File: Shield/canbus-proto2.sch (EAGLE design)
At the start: 81 parts, among them J1 Digital_0_7, J2 Analog, J3 Digital_8_13, J4 Analog, J5 Digital_14_21

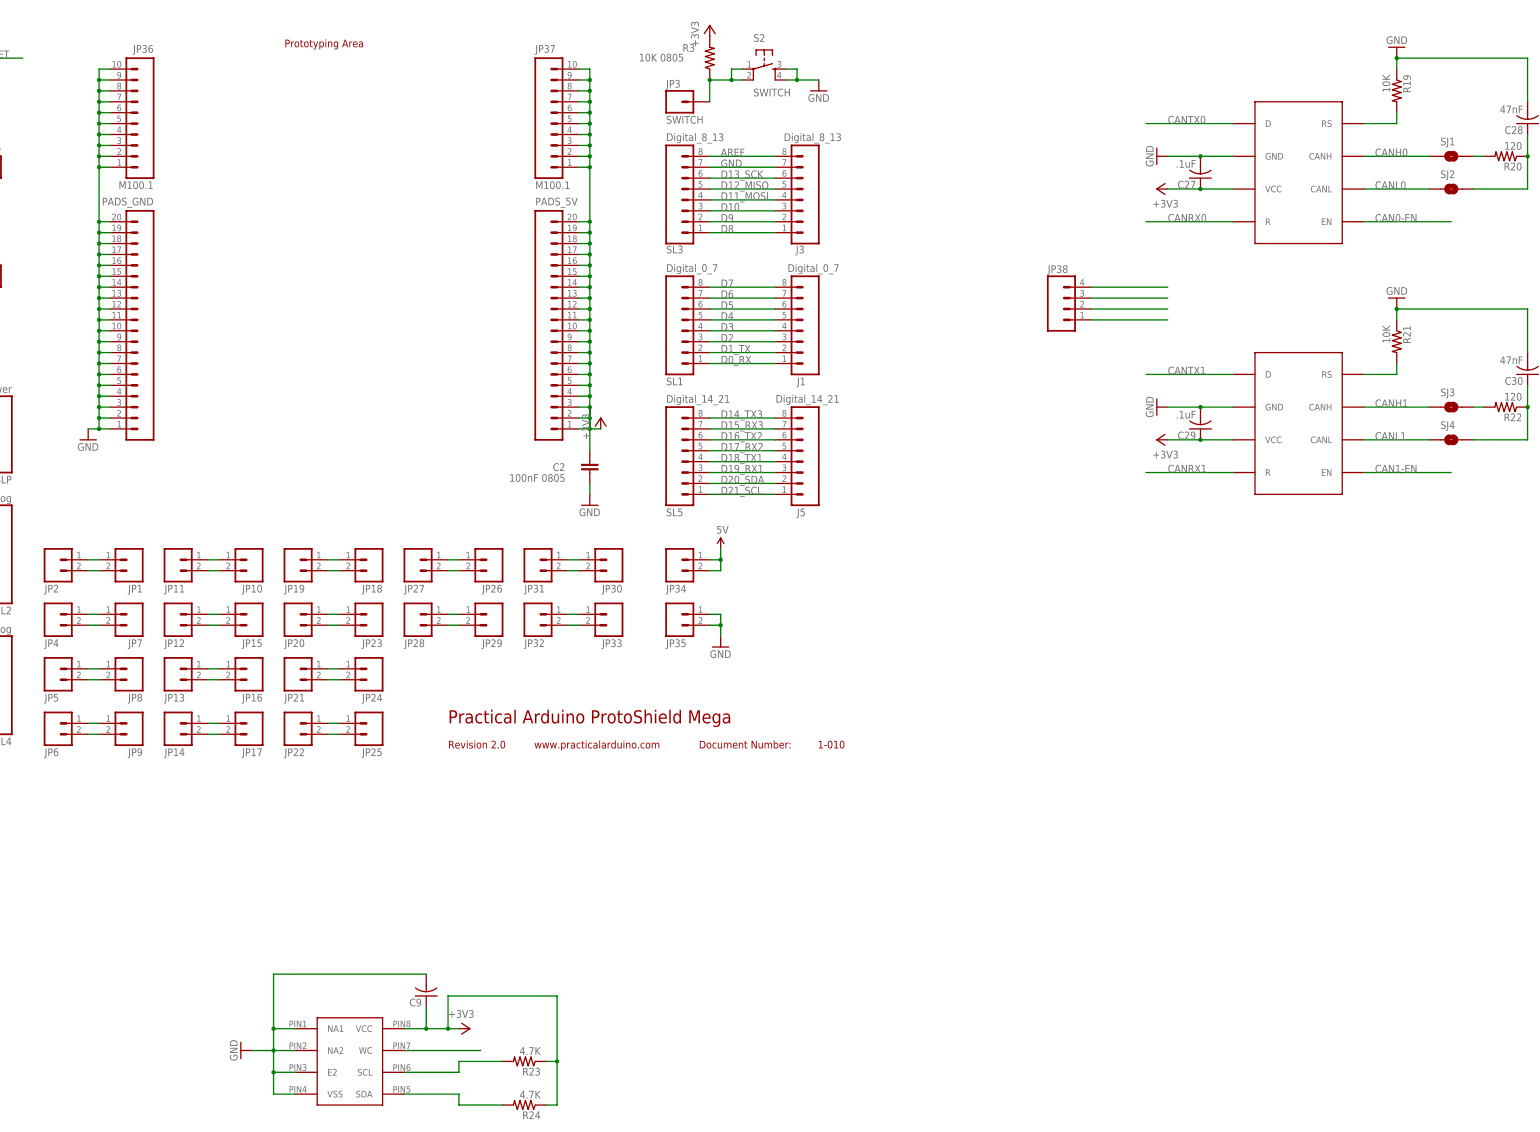
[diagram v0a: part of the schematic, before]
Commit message: Updated board design for canbus shield. There are now RJ45 ports for canbus outputs and a little SMD proto space.
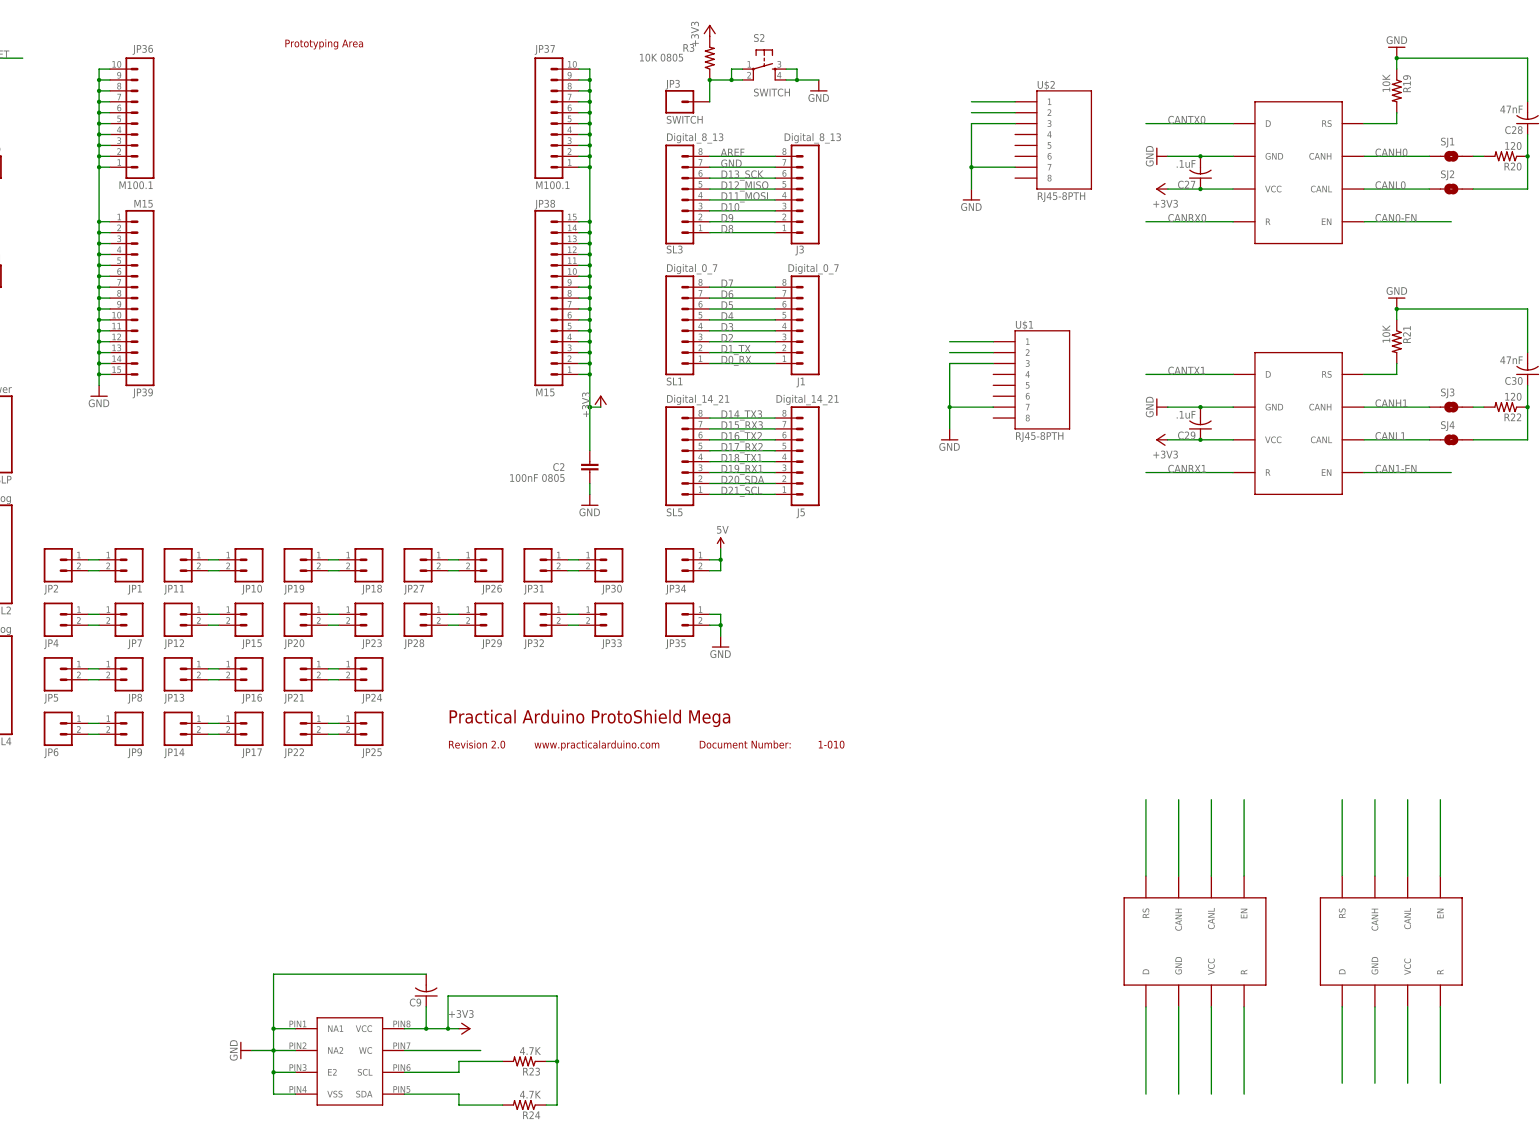
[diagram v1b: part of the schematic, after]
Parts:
- removed PADS_5V, PADS_GND: M20, SparkFun:M20
- added JP39: M15, SparkFun-Connectors:M15
- added U$1, U$2: RJ45-8PTH, SparkFun-Connectors:RJ45-8PTH
- added U$3, U$4: SN65HVD234, ck_custom:SN65HVD234
- JP38: value (none) -> M15; device SparkFun-Connectors:M04PTH -> SparkFun-Connectors:M15
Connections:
- new net B1: U$3.RS
- new net B10: U$4.CANH
- new net B11: U$4.CANL
- new net B12: U$4.EN
- new net B13: U$4.R
- new net B14: U$4.VCC
- new net B15: U$4.GND
- new net B16: U$4.D
- new net B2: U$3.CANH
- new net B3: U$3.CANL
- new net B4: U$3.EN
- new net B5: U$3.D
- new net B6: U$3.GND
- new net B7: U$3.VCC
- new net B8: U$3.R
- new net B9: U$4.RS
- net +3V3: now also JP38.1, JP38.10, JP38.11, JP38.12, JP38.13, JP38.14, JP38.15, JP38.2, JP38.3, JP38.4, JP38.5, JP38.6, JP38.7, JP38.8, JP38.9; no longer PADS_5V.1, PADS_5V.10, PADS_5V.11, PADS_5V.12, PADS_5V.13, PADS_5V.14, PADS_5V.15, PADS_5V.16, PADS_5V.17, PADS_5V.18, PADS_5V.19, PADS_5V.2, PADS_5V.20, PADS_5V.3, PADS_5V.4, PADS_5V.5, PADS_5V.6, PADS_5V.7, PADS_5V.8, PADS_5V.9
- net CANH0: now also U$2.1; no longer JP38.2
- net CANH1: now also U$1.1; no longer JP38.4
- net CANL0: now also U$2.2; no longer JP38.1
- net CANL1: now also U$1.2; no longer JP38.3
- net GND: now also JP39.1, JP39.10, JP39.11, JP39.12, JP39.13, JP39.14, JP39.15, JP39.2, JP39.3, JP39.4, JP39.5, JP39.6, JP39.7, JP39.8, JP39.9, U$1.3, U$1.7, U$2.3, U$2.7; no longer PADS_GND.1, PADS_GND.10, PADS_GND.11, PADS_GND.12, PADS_GND.13, PADS_GND.14, PADS_GND.15, PADS_GND.16, PADS_GND.17, PADS_GND.18, PADS_GND.19, PADS_GND.2, PADS_GND.20, PADS_GND.3, PADS_GND.4, PADS_GND.5, PADS_GND.6, PADS_GND.7, PADS_GND.8, PADS_GND.9

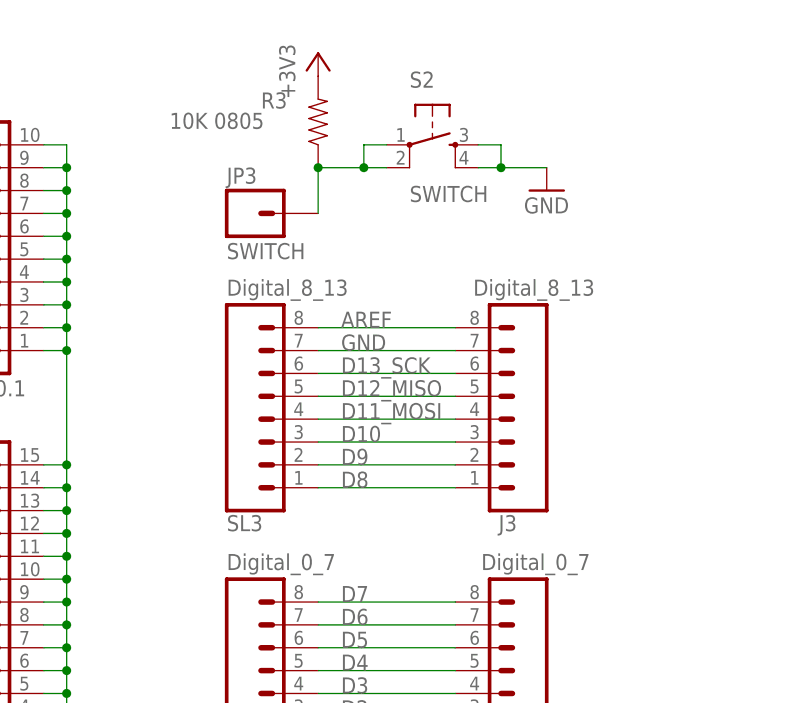
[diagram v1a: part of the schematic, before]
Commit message: Removed momentary switch, added SCL1/SDA1
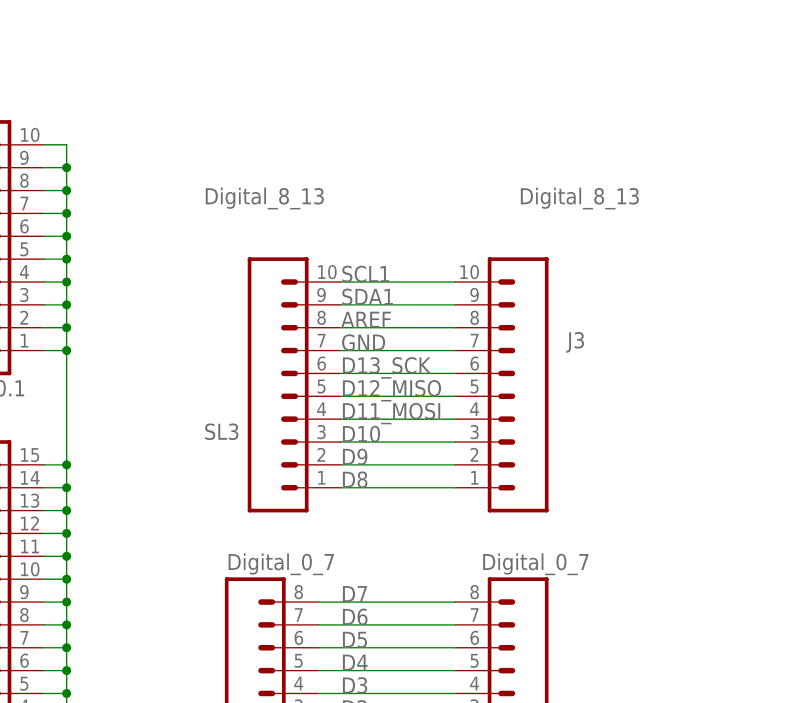
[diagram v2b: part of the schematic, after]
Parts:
- removed JP3: SWITCH, SparkFun:M01PTH
- removed R3: 10K 0805, SparkFun:RESISTOR0805-LARGE
- removed S2: SWITCH, SparkFun:TAC_SWITCHPTH
- J3, SL3: device SparkFun:M08 -> SparkFun-Connectors:M10"
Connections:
- removed net N$6: JP3.1, R3.1, S2.1, S2.2
- new net SCL1: J3.10, SL3.10
- new net SDA1: J3.9, SL3.9
- net +3V3: no longer R3.2
- net GND: no longer S2.3, S2.4
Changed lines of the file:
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@@
 <part name="SL2" library="SparkFun" deviceset="M08" device="" value="Analog"/>
 <part name="J1" library="SparkFun" deviceset="M08" device="" value="Digital_0_7"/>
-<part name="J3" library="SparkFun" deviceset="M08" device="" value="Digital_8_13"/>
-<part name="SL3" library="SparkFun" deviceset="M08" device="" value="Digital_8_13"/>
+<part name="J3" library="SparkFun-Connectors" deviceset="M10" device="&quot;" value="Digital_8_13"/>
+<part name="SL3" library="SparkFun-Connectors" deviceset="M10" device="&quot;" value="Digital_8_13"/>
 <part name="SL1" library="SparkFun" deviceset="M08" device="" value="Digital_0_7"/>
 <part name="C1" library="SparkFun" deviceset="CAP" device="0805-LARGE" value="100nF 0805"/>
@@
 <part name="R1" library="SparkFun" deviceset="RESISTOR" device="0805-LARGE" value="1K 0805"/>
 <part name="R2" library="SparkFun" deviceset="RESISTOR" device="0805-LARGE" value="1K 0805"/>
-<part name="R3" library="SparkFun" deviceset="RESISTOR" device="0805-LARGE" value="10K 0805"/>
 <part name="S1" library="SparkFun" deviceset="TAC_SWITCH" device="PTH" value="RESET"/>
-<part name="S2" library="SparkFun" deviceset="TAC_SWITCH" device="PTH" value="SWITCH"/>
 <part name="GND1" library="SparkFun" deviceset="GND" device=""/>
 <part name="GND2" library="SparkFun" deviceset="GND" device=""/>
 <part name="GND3" library="SparkFun" deviceset="GND" device=""/>
 <part name="GND4" library="SparkFun" deviceset="GND" device=""/>
-<part name="GND5" library="SparkFun" deviceset="GND" device=""/>
 <part name="RED" library="SparkFun" deviceset="M01" device="PTH" value=""/>
 <part name="GREEN" library="SparkFun" deviceset="M01" device="PTH" value=""/>
-<part name="JP3" library="SparkFun" deviceset="M01" device="PTH" value="SWITCH"/>
 <part name="J4" library="SparkFun" deviceset="M08" device="" value="Analog"/>
 <part name="SL4" library="SparkFun" deviceset="M08" device="" value="Analog"/>
@@
 <part name="R23" library="rcl" deviceset="R-US_" device="R0603" value="4.7K"/>
 <part name="R24" library="rcl" deviceset="R-US_" device="R0603" value="4.7K"/>
-<part name="+3V1" library="supply1" deviceset="+3V3" device=""/>
 <part name="+3V3" library="supply1" deviceset="+3V3" device=""/>
 <part name="+3V6" library="supply1" deviceset="+3V3" device=""/>
@@
 <attribute name="VALUE" x="238.506" y="117.856" size="1.778" layer="96" rot="MR0"/>
 </instance>
-<instance part="J3" gate="G$1" x="228.6" y="134.62" smashed="yes" rot="MR0">
-<attribute name="NAME" x="230.378" y="122.174" size="1.778" layer="95" rot="MR0"/>
-<attribute name="VALUE" x="239.014" y="148.336" size="1.778" layer="96" rot="MR0"/>
+<instance part="J3" gate="G$1" x="233.68" y="144.78" smashed="yes" rot="MR0">
+<attribute name="NAME" x="237.998" y="142.494" size="1.778" layer="95" rot="MR0"/>
+<attribute name="VALUE" x="244.094" y="158.496" size="1.778" layer="96" rot="MR0"/>
 </instance>
-<instance part="SL3" gate="G$1" x="203.2" y="134.62" smashed="yes">
-<attribute name="NAME" x="198.12" y="122.174" size="1.778" layer="95"/>
-<attribute name="VALUE" x="198.12" y="148.336" size="1.778" layer="96"/>
+<instance part="SL3" gate="G$1" x="200.66" y="144.78" smashed="yes">
+<attribute name="NAME" x="195.58" y="132.334" size="1.778" layer="95"/>
+<attribute name="VALUE" x="195.58" y="158.496" size="1.778" layer="96"/>
 </instance>
 <instance part="SL1" gate="G$1" x="203.2" y="104.14" smashed="yes">
@@
 <instance part="R1" gate="G$1" x="25.4" y="154.94"/>
 <instance part="R2" gate="G$1" x="25.4" y="129.54"/>
-<instance part="R3" gate="G$1" x="208.28" y="167.64" smashed="yes" rot="R90">
-<attribute name="NAME" x="201.93" y="169.1386" size="1.778" layer="95"/>
-<attribute name="VALUE" x="191.77" y="166.878" size="1.778" layer="96"/>
-</instance>
 <instance part="S1" gate="S" x="27.94" y="170.18"/>
-<instance part="S2" gate="S" x="220.98" y="165.1"/>
 <instance part="GND1" gate="1" x="38.1" y="96.52"/>
 <instance part="GND2" gate="1" x="180.34" y="63.5"/>
 <instance part="GND3" gate="1" x="66.04" y="88.9"/>
 <instance part="GND4" gate="1" x="15.24" y="165.1"/>
-<instance part="GND5" gate="1" x="233.68" y="160.02"/>
 <instance part="RED" gate="G$1" x="40.64" y="142.24" rot="MR0"/>
 <instance part="GREEN" gate="G$1" x="40.64" y="116.84" rot="MR0"/>
-<instance part="JP3" gate="G$1" x="200.66" y="157.48"/>
 <instance part="J4" gate="G$1" x="17.78" y="22.86" rot="MR180"/>
 <instance part="SL4" gate="G$1" x="40.64" y="22.86" rot="R180"/>
@@
 <instance part="R23" gate="G$1" x="165.1" y="-66.04" rot="R180"/>
 <instance part="R24" gate="G$1" x="165.1" y="-76.2" rot="R180"/>
-<instance part="+3V1" gate="G$1" x="208.28" y="175.26"/>
 <instance part="+3V3" gate="G$1" x="15.24" y="157.48"/>
 <instance part="+3V6" gate="G$1" x="182.88" y="88.9"/>
@@
 </segment>
 <segment>
-<wire x1="208.28" y1="142.24" x2="223.52" y2="142.24" width="0.1524" layer="91"/>
+<wire x1="210.82" y1="142.24" x2="223.52" y2="142.24" width="0.1524" layer="91"/>
 <label x="210.82" y="142.24" size="1.778" layer="95"/>
 <pinref part="SL3" gate="G$1" pin="7"/>
@@
 </segment>
 <segment>
-<wire x1="226.06" y1="165.1" x2="228.6" y2="165.1" width="0.1524" layer="91"/>
-<wire x1="228.6" y1="165.1" x2="228.6" y2="162.56" width="0.1524" layer="91"/>
-<wire x1="228.6" y1="162.56" x2="226.06" y2="162.56" width="0.1524" layer="91"/>
-<wire x1="228.6" y1="162.56" x2="233.68" y2="162.56" width="0.1524" layer="91"/>
-<junction x="228.6" y="162.56"/>
-<pinref part="S2" gate="S" pin="3"/>
-<pinref part="S2" gate="S" pin="4"/>
-<pinref part="GND5" gate="1" pin="GND"/>
-</segment>
-<segment>
 <wire x1="208.28" y1="38.1" x2="210.82" y2="38.1" width="0.2032" layer="91"/>
 <wire x1="210.82" y1="38.1" x2="210.82" y2="35.56" width="0.2032" layer="91"/>
@@
 <net name="AREF" class="0">
 <segment>
-<wire x1="208.28" y1="144.78" x2="223.52" y2="144.78" width="0.1524" layer="91"/>
+<wire x1="210.82" y1="144.78" x2="223.52" y2="144.78" width="0.1524" layer="91"/>
 <label x="210.82" y="144.78" size="1.778" layer="95"/>
 <pinref part="SL3" gate="G$1" pin="8"/>
@@
 <net name="D13_SCK" class="0">
 <segment>
-<wire x1="208.28" y1="139.7" x2="223.52" y2="139.7" width="0.1524" layer="91"/>
+<wire x1="210.82" y1="139.7" x2="223.52" y2="139.7" width="0.1524" layer="91"/>
 <label x="210.82" y="139.7" size="1.778" layer="95"/>
 <pinref part="SL3" gate="G$1" pin="6"/>
@@
 <net name="D12_MISO" class="0">
 <segment>
-<wire x1="208.28" y1="137.16" x2="223.52" y2="137.16" width="0.1524" layer="91"/>
+<wire x1="210.82" y1="137.16" x2="223.52" y2="137.16" width="0.1524" layer="91"/>
 <label x="210.82" y="137.16" size="1.778" layer="95"/>
 <pinref part="SL3" gate="G$1" pin="5"/>
@@
 <net name="D11_MOSI" class="0">
 <segment>
-<wire x1="223.52" y1="134.62" x2="208.28" y2="134.62" width="0.1524" layer="91"/>
+<wire x1="223.52" y1="134.62" x2="210.82" y2="134.62" width="0.1524" layer="91"/>
 <label x="210.82" y="134.62" size="1.778" layer="95"/>
 <pinref part="J3" gate="G$1" pin="4"/>
@@
 <net name="D10" class="0">
 <segment>
-<wire x1="208.28" y1="132.08" x2="223.52" y2="132.08" width="0.1524" layer="91"/>
+<wire x1="210.82" y1="132.08" x2="223.52" y2="132.08" width="0.1524" layer="91"/>
 <label x="210.82" y="132.08" size="1.778" layer="95"/>
 <pinref part="SL3" gate="G$1" pin="3"/>
@@
 <net name="D9" class="0">
 <segment>
-<wire x1="208.28" y1="129.54" x2="223.52" y2="129.54" width="0.1524" layer="91"/>
+<wire x1="210.82" y1="129.54" x2="223.52" y2="129.54" width="0.1524" layer="91"/>
 <label x="210.82" y="129.54" size="1.778" layer="95"/>
 <pinref part="SL3" gate="G$1" pin="2"/>
@@
 <net name="D8" class="0">
 <segment>
-<wire x1="208.28" y1="127" x2="223.52" y2="127" width="0.1524" layer="91"/>
+<wire x1="210.82" y1="127" x2="223.52" y2="127" width="0.1524" layer="91"/>
 <label x="210.82" y="127" size="1.778" layer="95"/>
 <pinref part="SL3" gate="G$1" pin="1"/>
@@
 <pinref part="SL1" gate="G$1" pin="1"/>
 <pinref part="J1" gate="G$1" pin="1"/>
-</segment>
-</net>
-<net name="N$6" class="0">
-<segment>
-<wire x1="215.9" y1="165.1" x2="213.36" y2="165.1" width="0.1524" layer="91"/>
-<wire x1="213.36" y1="165.1" x2="213.36" y2="162.56" width="0.1524" layer="91"/>
-<wire x1="213.36" y1="162.56" x2="215.9" y2="162.56" width="0.1524" layer="91"/>
-<wire x1="208.28" y1="157.48" x2="208.28" y2="162.56" width="0.1524" layer="91"/>
-<wire x1="213.36" y1="162.56" x2="208.28" y2="162.56" width="0.1524" layer="91"/>
-<junction x="213.36" y="162.56"/>
-<junction x="208.28" y="162.56"/>
-<pinref part="S2" gate="S" pin="1"/>
-<pinref part="S2" gate="S" pin="2"/>
-<pinref part="JP3" gate="G$1" pin="1"/>
-<pinref part="R3" gate="G$1" pin="1"/>
 </segment>
 </net>
@@
 <pinref part="+3V3" gate="G$1" pin="+3V3"/>
 <junction x="15.24" y="154.94"/>
-</segment>
-<segment>
-<pinref part="R3" gate="G$1" pin="2"/>
-<pinref part="+3V1" gate="G$1" pin="+3V3"/>
 </segment>
 <segment>
@@
 </segment>
 </net>
+<net name="SDA1" class="0">
+<segment>
+<pinref part="SL3" gate="G$1" pin="9"/>
+<pinref part="J3" gate="G$1" pin="9"/>
+<wire x1="210.82" y1="147.32" x2="223.52" y2="147.32" width="0.1524" layer="91"/>
+<label x="210.82" y="147.32" size="1.778" layer="95"/>
+</segment>
+</net>
+<net name="SCL1" class="0">
+<segment>
+<pinref part="SL3" gate="G$1" pin="10"/>
+<pinref part="J3" gate="G$1" pin="10"/>
+<wire x1="210.82" y1="149.86" x2="223.52" y2="149.86" width="0.1524" layer="91"/>
+<label x="210.82" y="149.86" size="1.778" layer="95"/>
+</segment>
+</net>
